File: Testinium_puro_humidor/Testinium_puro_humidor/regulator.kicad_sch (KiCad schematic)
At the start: 0 parts

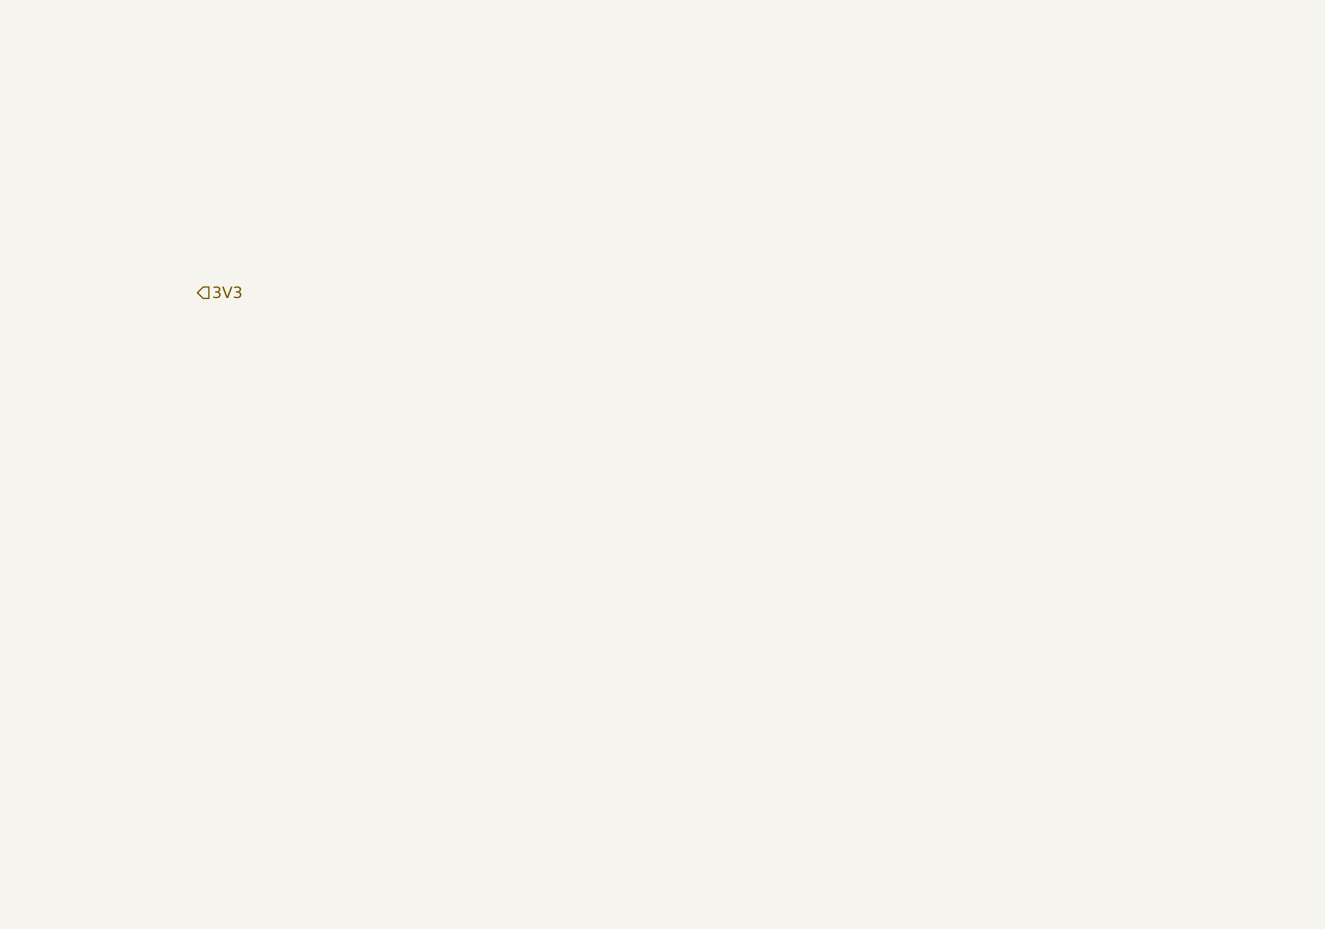
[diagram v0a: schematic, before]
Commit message: fan , uv led ,regülator devresi eklendi. piezo ve sarj devresi kaldi
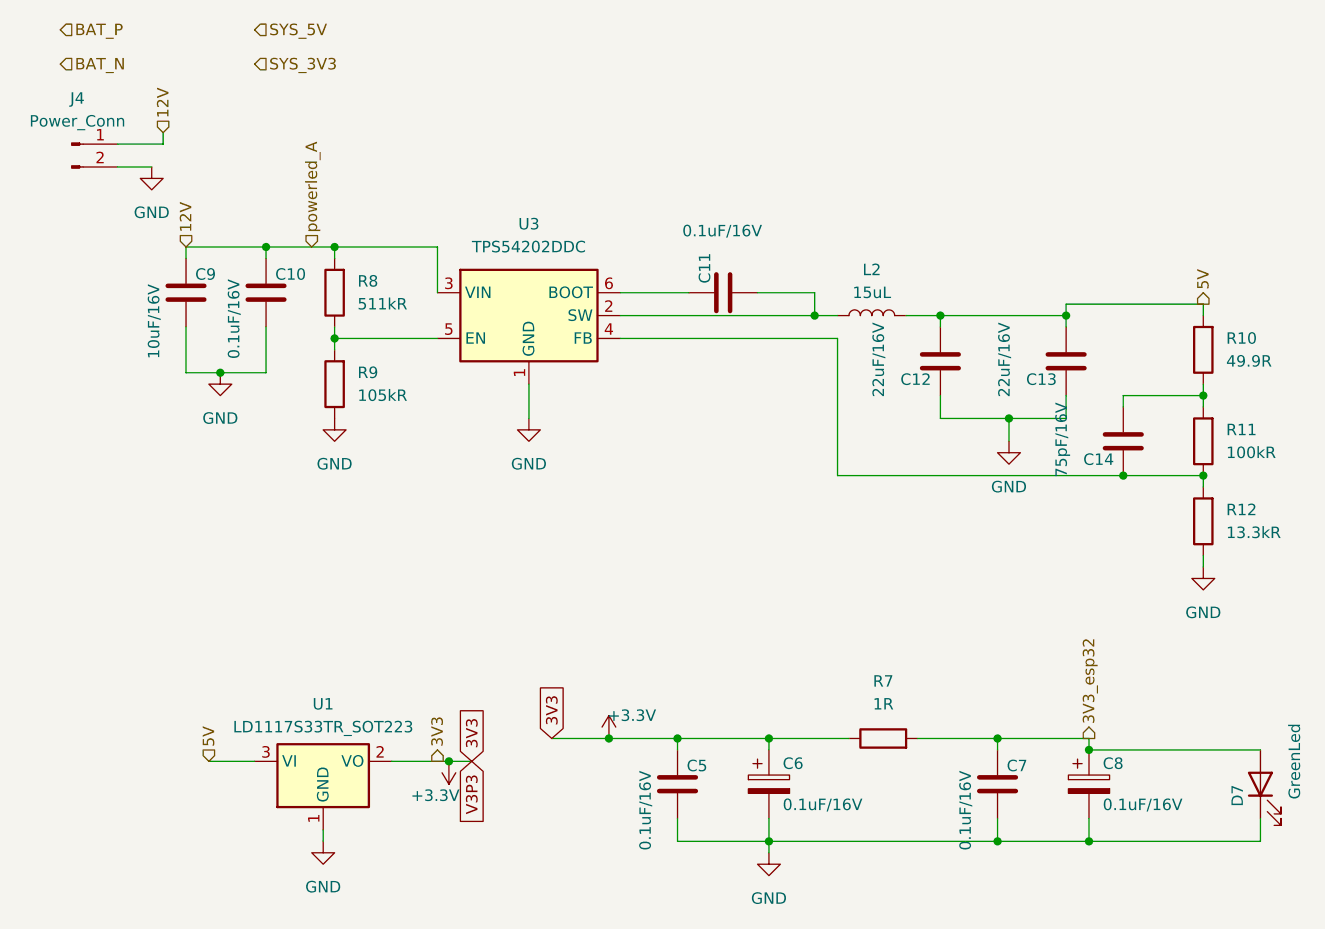
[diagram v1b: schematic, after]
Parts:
- added C10, C11, C5, C7: 0.1uF/16V, Capacitor_SMD:C_0805_2012Metric, symbol Device:C
- added C12, C13: 22uF/16V, Capacitor_SMD:C_0805_2012Metric, symbol Device:C
- added C14: 75pF/16V, Capacitor_SMD:C_0805_2012Metric, symbol Device:C
- added C6, C8: 0.1uF/16V, Capacitor_SMD:C_0805_2012Metric, symbol Device:C_Polarized
- added C9: 10uF/16V, Capacitor_SMD:C_0805_2012Metric, symbol Device:C
- added D7: GreenLed, LED_SMD:LED_0805_2012Metric, symbol Device:LED
- added J4: Power_Conn, Connector_JST:JST_EH_B2B-EH-A_1x02_P2.50mm_Vertical, symbol Connector:Conn_01x02_Pin
- added L2: 15uL, Inductor_SMD:L_Coilcraft_0805HQ_2012Metric, symbol Device:L
- added R10: 49.9R, Resistor_SMD:R_0603_1608Metric, symbol Device:R
- added R11: 100kR, Resistor_SMD:R_0603_1608Metric, symbol Device:R
- added R12: 13.3kR, Resistor_SMD:R_0603_1608Metric, symbol Device:R
- added R7: 1R, Resistor_SMD:R_0603_1608Metric, symbol Device:R
- added R8: 511kR, Resistor_SMD:R_0603_1608Metric, symbol Device:R
- added R9: 105kR, Resistor_SMD:R_0603_1608Metric, symbol Device:R
- added U1: LD1117S33TR_SOT223, Package_TO_SOT_SMD:SOT-223-3_TabPin2, symbol Regulator_Linear:LD1117S33TR_SOT223
- added U3: TPS54202DDC, baraysan:SOT95P280X110-6N, symbol Regulator_Switching:TPS54202DDC
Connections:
- new net: C14.1, R11.1, R12.2, U3.4 (FB)
- new net: C14.2, R10.1, R11.2
- new net: C11.2, L2.1, U3.2 (SW)
- new net: R8.1, R9.2, U3.5 (EN)
- new net: C11.1, U3.6 (BOOT)
- new net +3.3V: C5.1, C6.1, R7.1, U1.2 (VO)
- new net 12V: C10.1, C9.1, J4.1 (Pin_1), R8.2, U3.3 (VIN)
- new net 3V3_esp32: C7.1, C8.1, D7.2 (A), R7.2
- new net 5V: C12.2, C13.2, L2.2, R10.2, U1.3 (VI)
- new net GND: C10.2, C12.1, C13.1, C5.2, C6.2, C7.2, C8.2, C9.2, D7.1 (K), J4.2 (Pin_2), R12.1, R9.1, U1.1 (GND), U3.1 (GND)

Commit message: sematik tamamlandi
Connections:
- net GND: now also J4.1 (Pin_1); no longer J4.2 (Pin_2)
- net +3.3V renamed 3V3
- net 12V renamed Power
- net Power: now also J4.2 (Pin_2); no longer J4.1 (Pin_1)
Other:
- moved on the sheet: U1
